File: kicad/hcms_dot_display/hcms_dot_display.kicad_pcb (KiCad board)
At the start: 4 copper layers, 35.5 x 39.9 mm, 52 parts, among them J1 Conn_01x12, J2 USB_C_Receptacle_USB2.0, J3 Conn_01x12, J4 Conn_01x11_Female, J5 Conn_01x11_Male, J6 Conn_01x12, J7 Conn_01x12, Q1 Q_PMOS_DSG, Q2 Q_PMOS_DSG, Q3 Q_PMOS_DSG, Q4 Q_PMOS_DSG, Q5 Q_PMOS_DSG, Q6 Q_PMOS_DSG, SW1 SW_DIP_x03, U1 ATtiny826-SXX, U2 FT231XS

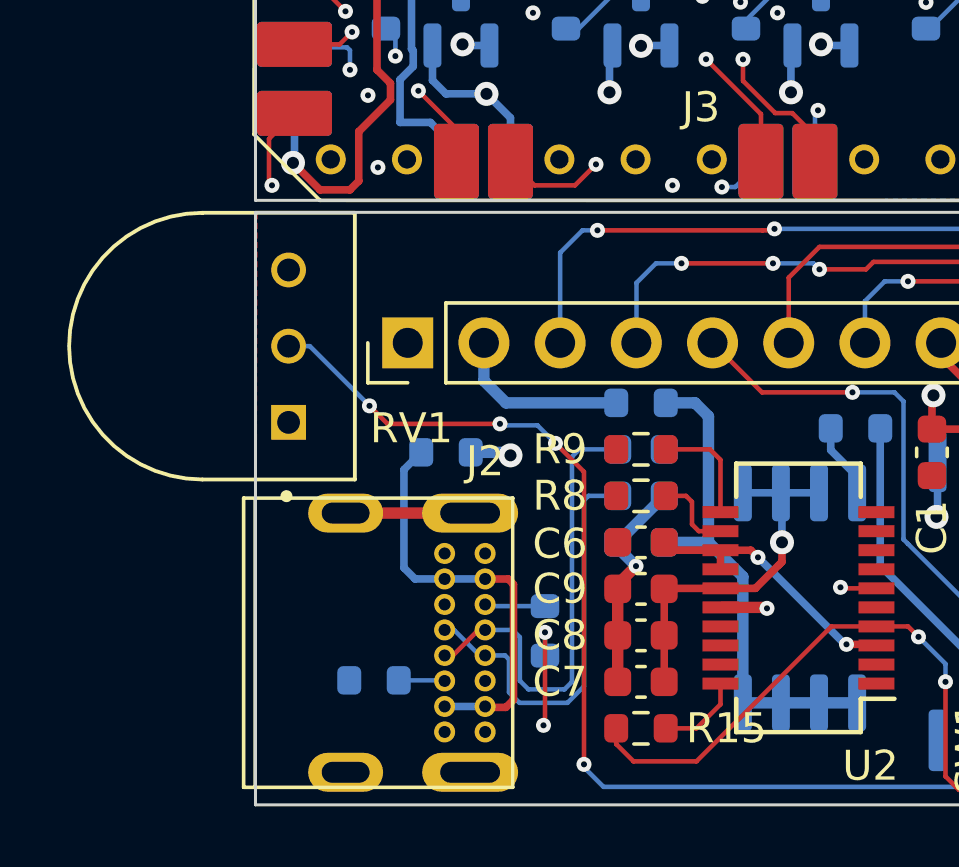
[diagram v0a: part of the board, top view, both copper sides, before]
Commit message: Fixed USB footprint to accomodate DRCs
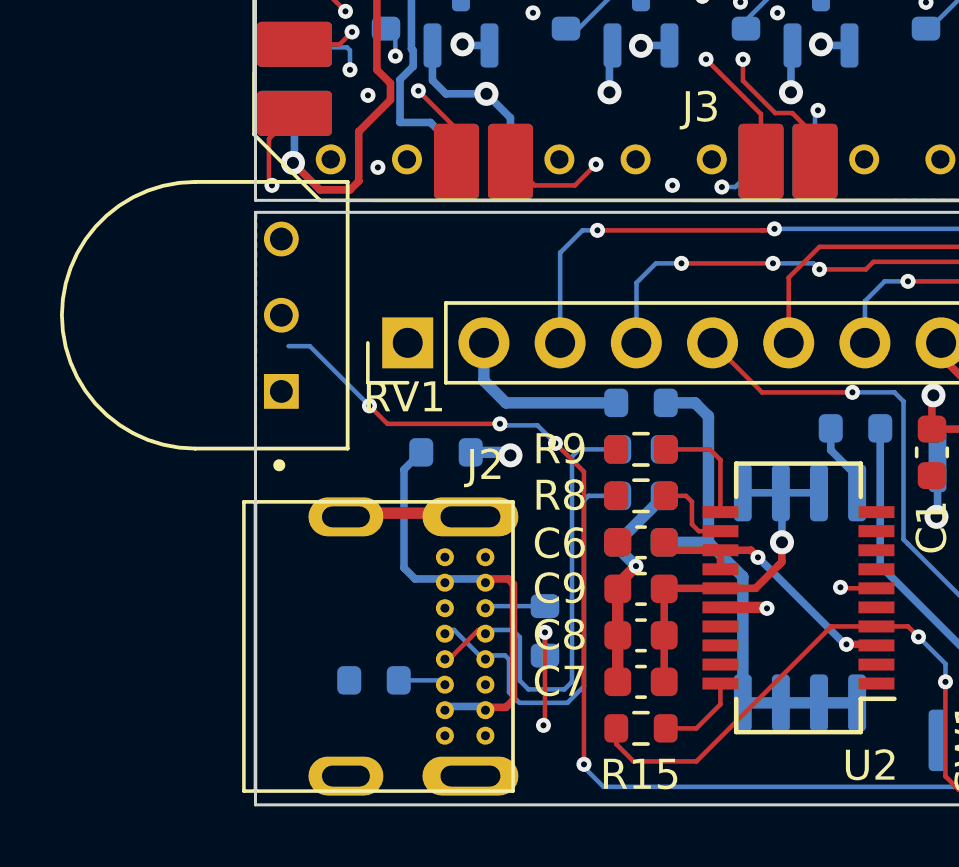
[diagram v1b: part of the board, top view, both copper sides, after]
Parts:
- moved RV1 1.06 mm to (160.7, 113.4)
- moved J2 0.13 mm to (166.8, 124.5)
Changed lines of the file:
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@@
   )
   (footprint "hcms:TRIM_3352T-1-201LF" (layer "F.Cu")
-    (at 160.982508 114.459995 90)
+    (at 160.7425 113.43 90)
     (property "DPN" " ")
     (property "PN" "3352T-1-503LF")
@@
     (property "Sheetname" "")
     (attr through_hole)
-    (fp_text reference "RV1" (at -2.74 6.9675 180) (layer "F.SilkS")
+    (fp_text reference "RV1" (at -2.74 6.9675) (layer "F.SilkS")
       (effects (font (size 1 1) (thickness 0.15)))
     )
@@
   )
   (footprint "hcms:213716-0001" (layer "F.Cu")
-    (at 166.840002 124.344989 -90)
+    (at 166.85 124.47 -90)
     (property "PN" "213716-0001")
     (property "Sheetfile" "hcms_dot_display.kicad_sch")
@@
       (effects (font (size 1 1) (thickness 0.15)))
     )
-    (fp_line (start 4.82 4.485) (end -4.82 4.485) (layer "F.SilkS") (width 0.12))
     (fp_line (start -4.8 4.1) (end 4.8 4.1) (layer "F.SilkS") (width 0.12))
     (fp_line (start -4.82 -4.485) (end 4.82 -4.485) (layer "F.SilkS") (width 0.12))
+    (fp_line (start 4.82 -4.485) (end 4.82 4.485) (layer "F.SilkS") (width 0.12))
+    (fp_line (start 4.82 4.485) (end -4.82 4.485) (layer "F.SilkS") (width 0.12))
     (fp_line (start -4.82 4.485) (end -4.82 -4.485) (layer "F.SilkS") (width 0.12))
-    (fp_line (start 4.82 -4.485) (end 4.82 4.485) (layer "F.SilkS") (width 0.12))
-    (fp_line (start -6.2 4.1) (end -5.1 4.1) (layer "Cmts.User") (width 0.12))
     (fp_line (start -5.1 4.1) (end -5.5 3.9) (layer "Cmts.User") (width 0.12))
     (fp_line (start -5.5 4.3) (end -5.1 4.1) (layer "Cmts.User") (width 0.12))
-    (pad "A1" thru_hole circle (at -2.975 -3.565 270) (size 0.7 0.7) (drill 0.4) (layers *.Cu *.Mask)
+    (fp_line (start -6.2 4.1) (end -5.1 4.1) (layer "Cmts.User") (width 0.12))
+    (pad "A1" thru_hole circle (at -2.975 -3.565 270) (size 0.6 0.6) (drill 0.3) (layers *.Cu *.Mask)
       (net 12 "GND") (pinfunction "GND") (pintype "passive"))
-    (pad "A4" thru_hole circle (at -2.125 -3.565 270) (size 0.7 0.7) (drill 0.4) (layers *.Cu *.Mask)
+    (pad "A4" thru_hole circle (at -2.125 -3.565 270) (size 0.6 0.6) (drill 0.3) (layers *.Cu *.Mask)
       (net 55 "Net-(J2-PadA4)") (pinfunction "VBUS") (pintype "passive"))
-    (pad "A5" thru_hole circle (at -1.275 -3.565 270) (size 0.7 0.7) (drill 0.4) (layers *.Cu *.Mask)
+    (pad "A5" thru_hole circle (at -1.275 -3.565 270) (size 0.6 0.6) (drill 0.3) (layers *.Cu *.Mask)
       (net 15 "Net-(J2-PadA5)") (pinfunction "CC1") (pintype "bidirectional"))
-    (pad "A6" thru_hole circle (at -0.425 -3.565 270) (size 0.7 0.7) (drill 0.4) (layers *.Cu *.Mask)
+    (pad "A6" thru_hole circle (at -0.425 -3.565 270) (size 0.6 0.6) (drill 0.3) (layers *.Cu *.Mask)
       (net 16 "/D+") (pinfunction "D+") (pintype "bidirectional"))
-    (pad "A7" thru_hole circle (at 0.425 -3.565 270) (size 0.7 0.7) (drill 0.4) (layers *.Cu *.Mask)
+    (pad "A7" thru_hole circle (at 0.425 -3.565 270) (size 0.6 0.6) (drill 0.3) (layers *.Cu *.Mask)
       (net 17 "/D-") (pinfunction "D-") (pintype "bidirectional"))
-    (pad "A8" thru_hole circle (at 1.275 -3.565 270) (size 0.7 0.7) (drill 0.4) (layers *.Cu *.Mask)
+    (pad "A8" thru_hole circle (at 1.275 -3.565 270) (size 0.6 0.6) (drill 0.3) (layers *.Cu *.Mask)
       (net 18 "unconnected-(J2-PadA8)") (pinfunction "SBU1") (pintype "bidirectional+no_connect"))
-    (pad "A9" thru_hole circle (at 2.125 -3.565 270) (size 0.7 0.7) (drill 0.4) (layers *.Cu *.Mask)
+    (pad "A9" thru_hole circle (at 2.125 -3.565 270) (size 0.6 0.6) (drill 0.3) (layers *.Cu *.Mask)
       (net 55 "Net-(J2-PadA4)") (pinfunction "VBUS") (pintype "passive"))
-    (pad "A12" thru_hole circle (at 2.975 -3.565 270) (size 0.7 0.7) (drill 0.4) (layers *.Cu *.Mask)
+    (pad "A12" thru_hole circle (at 2.975 -3.565 270) (size 0.6 0.6) (drill 0.3) (layers *.Cu *.Mask)
       (net 12 "GND") (pinfunction "GND") (pintype "passive"))
-    (pad "B1" thru_hole circle (at 2.975 -2.215 270) (size 0.7 0.7) (drill 0.4) (layers *.Cu *.Mask)
+    (pad "B1" thru_hole circle (at 2.975 -2.215 270) (size 0.6 0.6) (drill 0.3) (layers *.Cu *.Mask)
       (net 12 "GND") (pinfunction "GND") (pintype "passive"))
-    (pad "B4" thru_hole circle (at 2.125 -2.215 270) (size 0.7 0.7) (drill 0.4) (layers *.Cu *.Mask)
+    (pad "B4" thru_hole circle (at 2.125 -2.215 270) (size 0.6 0.6) (drill 0.3) (layers *.Cu *.Mask)
       (net 55 "Net-(J2-PadA4)") (pinfunction "VBUS") (pintype "passive"))
-    (pad "B5" thru_hole circle (at 1.275 -2.215 270) (size 0.7 0.7) (drill 0.4) (layers *.Cu *.Mask)
+    (pad "B5" thru_hole circle (at 1.275 -2.215 270) (size 0.6 0.6) (drill 0.3) (layers *.Cu *.Mask)
       (net 19 "Net-(J2-PadB5)") (pinfunction "CC2") (pintype "bidirectional"))
-    (pad "B6" thru_hole circle (at 0.425 -2.215 270) (size 0.7 0.7) (drill 0.4) (layers *.Cu *.Mask)
+    (pad "B6" thru_hole circle (at 0.425 -2.215 270) (size 0.6 0.6) (drill 0.3) (layers *.Cu *.Mask)
       (net 16 "/D+") (pinfunction "D+") (pintype "bidirectional"))
-    (pad "B7" thru_hole circle (at -0.425 -2.215 270) (size 0.7 0.7) (drill 0.4) (layers *.Cu *.Mask)
+    (pad "B7" thru_hole circle (at -0.425 -2.215 270) (size 0.6 0.6) (drill 0.3) (layers *.Cu *.Mask)
       (net 17 "/D-") (pinfunction "D-") (pintype "bidirectional"))
-    (pad "B8" thru_hole circle (at -1.275 -2.215 270) (size 0.7 0.7) (drill 0.4) (layers *.Cu *.Mask)
+    (pad "B8" thru_hole circle (at -1.275 -2.215 270) (size 0.6 0.6) (drill 0.3) (layers *.Cu *.Mask)
       (net 20 "unconnected-(J2-PadB8)") (pinfunction "SBU2") (pintype "bidirectional+no_connect"))
-    (pad "B9" thru_hole circle (at -2.125 -2.215 270) (size 0.7 0.7) (drill 0.4) (layers *.Cu *.Mask)
+    (pad "B9" thru_hole circle (at -2.125 -2.215 270) (size 0.6 0.6) (drill 0.3) (layers *.Cu *.Mask)
       (net 55 "Net-(J2-PadA4)") (pinfunction "VBUS") (pintype "passive"))
-    (pad "B12" thru_hole circle (at -2.975 -2.215 270) (size 0.7 0.7) (drill 0.4) (layers *.Cu *.Mask)
+    (pad "B12" thru_hole circle (at -2.975 -2.215 270) (size 0.6 0.6) (drill 0.3) (layers *.Cu *.Mask)
       (net 12 "GND") (pinfunction "GND") (pintype "passive"))
+    (pad "S1" thru_hole oval (at -4.32 -3.065 270) (size 1.3 3.2) (drill oval 0.7 2) (layers *.Cu *.Mask)
+      (net 12 "GND") (pinfunction "SHIELD") (pintype "passive"))
     (pad "S1" thru_hole oval (at 4.32 1.085 270) (size 1.3 2.5) (drill oval 0.7 1.6) (layers *.Cu *.Mask)
-      (net 12 "GND") (pinfunction "SHIELD") (pintype "passive"))
-    (pad "S1" thru_hole oval (at 4.32 -3.065 270) (size 1.3 3.2) (drill oval 0.7 2) (layers *.Cu *.Mask)
       (net 12 "GND") (pinfunction "SHIELD") (pintype "passive"))
     (pad "S1" thru_hole oval (at -4.32 1.085 270) (size 1.3 2.5) (drill oval 0.7 1.6) (layers *.Cu *.Mask)
       (net 12 "GND") (pinfunction "SHIELD") (pintype "passive"))
-    (pad "S1" thru_hole oval (at -4.32 -3.065 270) (size 1.3 3.2) (drill oval 0.7 2) (layers *.Cu *.Mask)
+    (pad "S1" thru_hole oval (at 4.32 -3.065 270) (size 1.3 3.2) (drill oval 0.7 2) (layers *.Cu *.Mask)
       (net 12 "GND") (pinfunction "SHIELD") (pintype "passive"))
     (model "${PROJECT_FOLDER}/hcms_dot_display/step/2137160001.stp"
@@
     (property "Sheetname" "")
     (attr smd)
-    (fp_text reference "R15" (at 2.85 0) (layer "F.SilkS")
+    (fp_text reference "R15" (at -0.02 1.55) (layer "F.SilkS")
       (effects (font (size 1 1) (thickness 0.15)))
     )
@@
     (property "Sheetname" "")
     (attr smd)
-    (fp_text reference "R21" (at 0 1.45) (layer "B.SilkS")
+    (fp_text reference "R21" (at 0.12 1.63) (layer "B.SilkS")
       (effects (font (size 1 1) (thickness 0.15)) (justify mirror))
     )
@@
     (effects (font (size 1 1) (thickness 0.15)) (justify left mirror))
   )
+  (target plus (at 219.88 120.12) (size 5) (width 0.1) (layer "Edge.Cuts"))
   (via (at 188.714002 99.860608) (size 0.5) (drill 0.2) (layers "F.Cu" "B.Cu") (net 1))
   (via (at 186.85 96.4) (size 0.5) (drill 0.2) (layers "F.Cu" "B.Cu") (net 1))

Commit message: ready for layout review
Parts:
- added REF**: MountingHole_2.2mm_M2_Pad_Via, MountingHole:MountingHole_2.2mm_M2_Pad_Via, F.Cu at (165.8, 125.2)
- moved RV1 39.6 mm to (200.3, 114.4), turned to -90 degrees
- moved R18 4.85 mm to (188.5, 118.0)
- moved R19 4.85 mm to (190.1, 118.0)
- moved R20 4.85 mm to (191.6, 118.0)
- moved R4 3.75 mm to (166.7, 121.8)
- moved U1 0.55 mm to (191.2, 123.5)
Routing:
- net /POT: track 37.3 -> 21.5 mm, vias 4 -> 3
- net /MCU_COL_5: track 87.2 -> 83.8 mm
- net Net-(J2-PadB5): track 1.54 -> 4.47 mm
- net /CONFIG_0: track 22.0 -> 19.5 mm
- net GND: track 69.8 -> 72.2 mm, vias 10 -> 9
- net /MCU_COL_4: track 100.1 -> 97.9 mm, vias 13 -> 15
- net /D+: track 15.5 -> 13.4 mm
- net /D-: track 13.9 -> 12.0 mm
- net /MCU_COL_3: track 94.1 -> 92.5 mm, vias 10 -> 12
- net /CONFIG_2: track 14.2 -> 13.4 mm
- net Net-(J2-PadA4): track 14.2 -> 13.6 mm
- net /UPDI: track 24.4 -> 25.0 mm
- net /MCU_COL_2: track 104.4 -> 103.9 mm, vias 9 -> 11
- net /MCU_COL_1: track 99.6 -> 99.5 mm, vias 10 -> 8

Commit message: layout ready for review i think
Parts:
- removed REF**: MountingHole_2.2mm_M2_Pad_Via, MountingHole:MountingHole_2.2mm_M2_Pad_Via
- added J8: Conn_01x02_Male, Connector_PinHeader_2.54mm:PinHeader_1x02_P2.54mm_Vertical, F.Cu at (164.5, 114.4)
- added MH1: MountingHole, MountingHole:MountingHole_2.2mm_M2_Pad_Via, F.Cu at (165.9, 125.1)
- added MH2: MountingHole, MountingHole:MountingHole_2.2mm_M2_Pad_Via, F.Cu at (192.8, 127.0)
- added R23: 0, Resistor_SMD:R_0603_1608Metric, F.Cu at (166.1, 111.5)
- U1: value ATtiny826-SXX -> ATtiny1626-X; footprint Package_SO:SOIC-20W_7.5x12.8mm_P1.27mm -> Package_SO:SSOP-20_5.3x7.2mm_P0.65mm
- moved C1 6.75 mm to (192.1, 118.1), turned to -90 degrees
- moved C2 3.60 mm to (190.5, 118.1), turned to -90 degrees
- moved U1 3.40 mm to (190.1, 120.3), turned to 180 degrees
- moved R18 3.05 mm to (185.4, 118.1)
- moved R19 3.05 mm to (187.0, 118.1)
- moved R20 3.05 mm to (188.6, 118.1)
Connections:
- U1 pad 2: /CONFIG_1 -> /CONFIG_2
- U1 pad 4: /CONFIG_2 -> /CONFIG_1
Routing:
- net /MCU_COL_1: track 99.5 -> 85.7 mm
- net /POT: track 21.5 -> 12.4 mm, vias 3 -> 1
- net /UPDI: track 25.0 -> 16.9 mm, vias 3 -> 1
- net /COL_PWM: track 11.7 -> 3.92 mm
- net GND: track 72.2 -> 66.1 mm, vias 9 -> 10
- net /MCU_DATA: track 9.72 -> 15.5 mm
- net /CONFIG_1: track 22.7 -> 17.0 mm
- net /MCU_COL_4: track 97.9 -> 103.4 mm, vias 15 -> 10
- net /MCU_COL_2: track 103.9 -> 108.1 mm, vias 11 -> 8
- net /CLK: track 85.9 -> 89.7 mm
- net +5V: track 79.3 -> 83.0 mm
- net Net-(J8-Pad1): track 0.00 -> 3.23 mm
- net /MCU_COL_3: track 92.5 -> 95.7 mm, vias 12 -> 10
- net /nBLNK: track 95.6 -> 98.8 mm, vias 6 -> 5
- net /MCU_COL_5: track 83.8 -> 81.2 mm, vias 7 -> 5
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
